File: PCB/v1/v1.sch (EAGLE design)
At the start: 64 parts, among them U2 AT24C512C-SHD-B

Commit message: push to work from main pc
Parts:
- removed R1, R2, R3, R4: (no value), resistor-shunt:BVS
- added R5, R6, R7, R8: (no value), eagle-ltspice:RR1206
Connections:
- net N$20: now also R7.1; no longer R1.2
- net N$36: now also R6.1; no longer R2.2
- net N$37: now also R7.2; no longer R1.1
- net N$38: now also R6.2; no longer R2.1
- net N$40: now also R8.1; no longer R4.2
- net N$45: now also R5.1; no longer R3.1
- net VDD: now also R5.2, R8.2; no longer R3.2, R4.1

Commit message: takes its time
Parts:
- removed PIO10, PIO11: (no value), wirepad:1,6/0,8
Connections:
- removed net N$42: PIO10.P, U$1.PIO[10]
- removed net N$47: PIO11.P, U$1.PIO[11]
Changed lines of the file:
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@@
 <part name="AIO0" library="wirepad" deviceset="1,6/0,8" device=""/>
 <part name="PIO3" library="wirepad" deviceset="1,6/0,8" device=""/>
-<part name="PIO10" library="wirepad" deviceset="1,6/0,8" device=""/>
-<part name="PIO11" library="wirepad" deviceset="1,6/0,8" device=""/>
 <part name="C1" library="AVX_By_element14_Batch_1" deviceset="UQCL2A100JAT2A/500" device="" value="1u"/>
 <part name="VPLUS" library="solpad" deviceset="LSP10" device="" value="Vrail"/>
@@
 <instance part="AIO0" gate="P" x="-55.88" y="15.24" rot="R90"/>
 <instance part="PIO3" gate="P" x="-33.02" y="10.16" rot="R90"/>
-<instance part="PIO10" gate="P" x="-20.32" y="81.28" rot="MR0"/>
-<instance part="PIO11" gate="P" x="-27.94" y="91.44" rot="R180"/>
 <instance part="C1" gate="A" x="73.152" y="108.204" rot="R90"/>
 <instance part="VPLUS" gate="1" x="-157.48" y="114.3" rot="R270"/>
@@
 </segment>
 </net>
-<net name="N$47" class="0">
-<segment>
-<pinref part="PIO11" gate="P" pin="P"/>
-<wire x1="-33.02" y1="91.44" x2="-30.48" y2="91.44" width="0.1524" layer="91"/>
-<pinref part="U$1" gate="G$1" pin="PIO[11]"/>
-</segment>
-</net>
 <net name="N$48" class="0">
 <segment>
@@
 </segment>
 </net>
-<net name="N$42" class="0">
-<segment>
-<pinref part="PIO10" gate="P" pin="P"/>
-<pinref part="U$1" gate="G$1" pin="PIO[10]"/>
-</segment>
-</net>

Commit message: getting there
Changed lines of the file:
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@@
 <wire x1="-129.54" y1="101.6" x2="-137.16" y2="101.6" width="0.1524" layer="91"/>
 <junction x="-137.16" y="101.6"/>
-<wire x1="-137.16" y1="101.6" x2="-144.78" y2="101.6" width="0.1524" layer="91"/>
 <pinref part="C19" gate="A" pin="C1"/>
 <wire x1="-154.94" y1="101.6" x2="-144.78" y2="101.6" width="0.1524" layer="91"/>
@@
 <junction x="-157.48" y="71.12"/>
 <pinref part="U$6" gate="G$1" pin="NEG"/>
+<wire x1="-144.78" y1="101.6" x2="-137.16" y2="101.6" width="0.1524" layer="91"/>
 </segment>
 <segment>

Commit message: quickly added antenna
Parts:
- added U$7: ANTENNA_1LEFT, ant-planar-1:ANTENNA_1LEFT
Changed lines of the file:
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@@
 <part name="R7" library="eagle-ltspice" deviceset="R" device="R1206"/>
 <part name="R8" library="eagle-ltspice" deviceset="R" device="R1206"/>
+<part name="U$7" library="ant-planar-1" deviceset="ANTENNA_1" device="LEFT"/>
 </parts>
 <sheets>
-<sheet>
-<plain>
-</plain>
-<instances>
-</instances>
-<busses>
-</busses>
-<nets>
-</nets>
-</sheet>
 <sheet>
 <plain>
@@
 <instance part="GND7" gate="1" x="-129.54" y="15.24"/>
 <instance part="C14" gate="A" x="-101.6" y="10.16" rot="R90"/>
-<instance part="GND9" gate="1" x="-165.1" y="27.94"/>
+<instance part="GND9" gate="1" x="-152.4" y="25.4"/>
 <instance part="C16" gate="A" x="-137.16" y="109.22" rot="R270"/>
 <instance part="C17" gate="A" x="-129.54" y="109.22" rot="R270"/>
@@
 <instance part="R7" gate="G$1" x="-48.26" y="-12.7" rot="R90"/>
 <instance part="R8" gate="G$1" x="30.48" y="-27.94" rot="R90"/>
+<instance part="U$7" gate="G$1" x="-157.48" y="45.72"/>
 </instances>
 <busses>
@@
 </segment>
 <segment>
+<pinref part="C10" gate="A" pin="C1"/>
+<pinref part="C11" gate="A" pin="C1"/>
+<wire x1="-137.16" y1="20.32" x2="-129.54" y2="20.32" width="0.1524" layer="91"/>
+<pinref part="GND7" gate="1" pin="GND"/>
+<wire x1="-129.54" y1="17.78" x2="-129.54" y2="20.32" width="0.1524" layer="91"/>
+<junction x="-129.54" y="20.32"/>
+<wire x1="-129.54" y1="20.32" x2="-121.92" y2="20.32" width="0.1524" layer="91"/>
+</segment>
+<segment>
 <pinref part="GND9" gate="1" pin="GND"/>
-<wire x1="-165.1" y1="35.56" x2="-165.1" y2="30.48" width="0.1524" layer="91"/>
+<wire x1="-152.4" y1="33.02" x2="-152.4" y2="27.94" width="0.1524" layer="91"/>
 </segment>
 <segment>
@@
 <wire x1="-83.82" y1="119.38" x2="-76.2" y2="119.38" width="0.1524" layer="91"/>
 <junction x="-76.2" y="119.38"/>
-</segment>
-<segment>
-<pinref part="C11" gate="A" pin="C1"/>
-<pinref part="C10" gate="A" pin="C1"/>
-<wire x1="-137.16" y1="20.32" x2="-129.54" y2="20.32" width="0.1524" layer="91"/>
-<pinref part="GND7" gate="1" pin="GND"/>
-<wire x1="-129.54" y1="20.32" x2="-121.92" y2="20.32" width="0.1524" layer="91"/>
-<wire x1="-129.54" y1="17.78" x2="-129.54" y2="20.32" width="0.1524" layer="91"/>
-<junction x="-129.54" y="20.32"/>
 </segment>
 </net>
@@
 <wire x1="-96.52" y1="35.56" x2="-109.22" y2="35.56" width="0.1524" layer="91"/>
 <pinref part="U$1" gate="G$1" pin="RF"/>
-</segment>
-</net>
+<wire x1="-109.22" y1="35.56" x2="-152.4" y2="35.56" width="0.1524" layer="91"/>
+<junction x="-109.22" y="35.56"/>
+</segment>
+</net>

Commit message: latest
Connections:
- net GND: now also U$5.NEG; no longer U$6.NEG
- net N$34: now also U$6.POS; no longer U$5.POS
- net N$48: now also U$5.POS, U$6.NEG; no longer U$5.NEG, U$6.POS
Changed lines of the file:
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@@
 <part name="U$2" library="MINI_SMT_8_PIN_CONNECTOR" deviceset="8PIN_SMT_CONNECTOR" device=""/>
 <part name="U$4" library="SSP-T7-F" deviceset="SSP-T7-F" device=""/>
-<part name="U$5" library="BATTERY_2996" deviceset="BATTERY_2996" device=""/>
-<part name="U$6" library="BATTERY_2996" deviceset="BATTERY_2996" device=""/>
 <part name="R5" library="eagle-ltspice" deviceset="R" device="R1206"/>
 <part name="R6" library="eagle-ltspice" deviceset="R" device="R1206"/>
@@
 <part name="R8" library="eagle-ltspice" deviceset="R" device="R1206"/>
 <part name="U$7" library="ant-planar-1" deviceset="ANTENNA_1" device="LEFT"/>
+<part name="U$5" library="BATTERY_2996" deviceset="BATTERY_2996" device=""/>
+<part name="U$6" library="BATTERY_2996" deviceset="BATTERY_2996" device=""/>
 </parts>
 <sheets>
@@
 <instance part="U$2" gate="G$1" x="43.18" y="-48.26"/>
 <instance part="U$4" gate="G$1" x="-109.22" y="69.85" rot="R270"/>
-<instance part="U$5" gate="G$1" x="-172.72" y="101.6"/>
-<instance part="U$6" gate="G$1" x="-172.72" y="78.74"/>
 <instance part="R5" gate="G$1" x="1.27" y="85.09"/>
 <instance part="R6" gate="G$1" x="-40.64" y="-12.7" rot="R90"/>
@@
 <instance part="R8" gate="G$1" x="30.48" y="-27.94" rot="R90"/>
 <instance part="U$7" gate="G$1" x="-157.48" y="45.72"/>
+<instance part="U$5" gate="G$1" x="-172.72" y="78.74"/>
+<instance part="U$6" gate="G$1" x="-172.72" y="101.6"/>
 </instances>
 <busses>
@@
 <pinref part="VGND" gate="1" pin="MP"/>
 <junction x="-157.48" y="71.12"/>
-<pinref part="U$6" gate="G$1" pin="NEG"/>
 <wire x1="-144.78" y1="101.6" x2="-137.16" y2="101.6" width="0.1524" layer="91"/>
+<pinref part="U$5" gate="G$1" pin="NEG"/>
 </segment>
 <segment>
@@
 <pinref part="U$1" gate="G$1" pin="VDD_PADS"/>
 <pinref part="U$1" gate="G$1" pin="VDD_BAT_SMPS"/>
-<pinref part="U$5" gate="G$1" pin="POS"/>
+<pinref part="U$6" gate="G$1" pin="POS"/>
 </segment>
 </net>
@@
 <segment>
 <wire x1="-162.56" y1="93.98" x2="-162.56" y2="86.36" width="0.1524" layer="91"/>
-<pinref part="U$5" gate="G$1" pin="NEG"/>
-<pinref part="U$6" gate="G$1" pin="POS"/>
-</segment>
-</net>
+<pinref part="U$5" gate="G$1" pin="POS"/>
+<pinref part="U$6" gate="G$1" pin="NEG"/>
+</segment>
+</net>

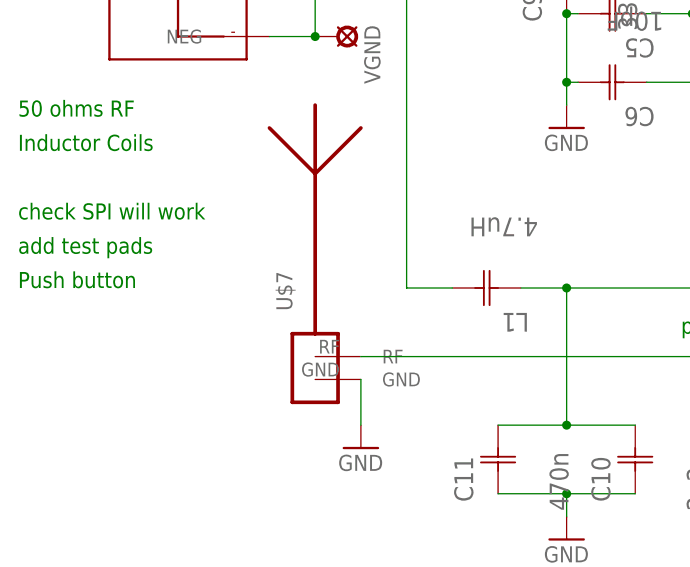
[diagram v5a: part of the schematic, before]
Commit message: expose pads more and add other ADC
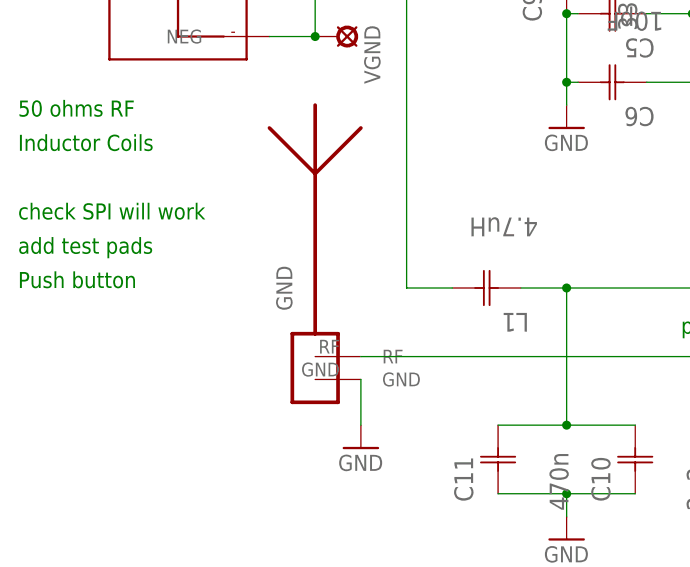
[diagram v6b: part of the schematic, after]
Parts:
- renumbered U$7 to GND
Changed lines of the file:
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@@
 <part name="R7" library="eagle-ltspice" deviceset="R" device="R1206"/>
 <part name="R8" library="eagle-ltspice" deviceset="R" device="R1206"/>
-<part name="U$7" library="ant-planar-1" deviceset="ANTENNA_1" device="LEFT"/>
+<part name="GND" library="ant-planar-1" deviceset="ANTENNA_1" device="LEFT"/>
 <part name="U$5" library="BATTERY_2996" deviceset="BATTERY_2996" device=""/>
 <part name="U$6" library="BATTERY_2996" deviceset="BATTERY_2996" device=""/>
@@
 <instance part="R7" gate="G$1" x="-48.26" y="-12.7" rot="R90"/>
 <instance part="R8" gate="G$1" x="30.48" y="-27.94" rot="R90"/>
-<instance part="U$7" gate="G$1" x="-157.48" y="45.72"/>
+<instance part="GND" gate="G$1" x="-157.48" y="45.72"/>
 <instance part="U$5" gate="G$1" x="-172.72" y="78.74"/>
 <instance part="U$6" gate="G$1" x="-172.72" y="101.6"/>

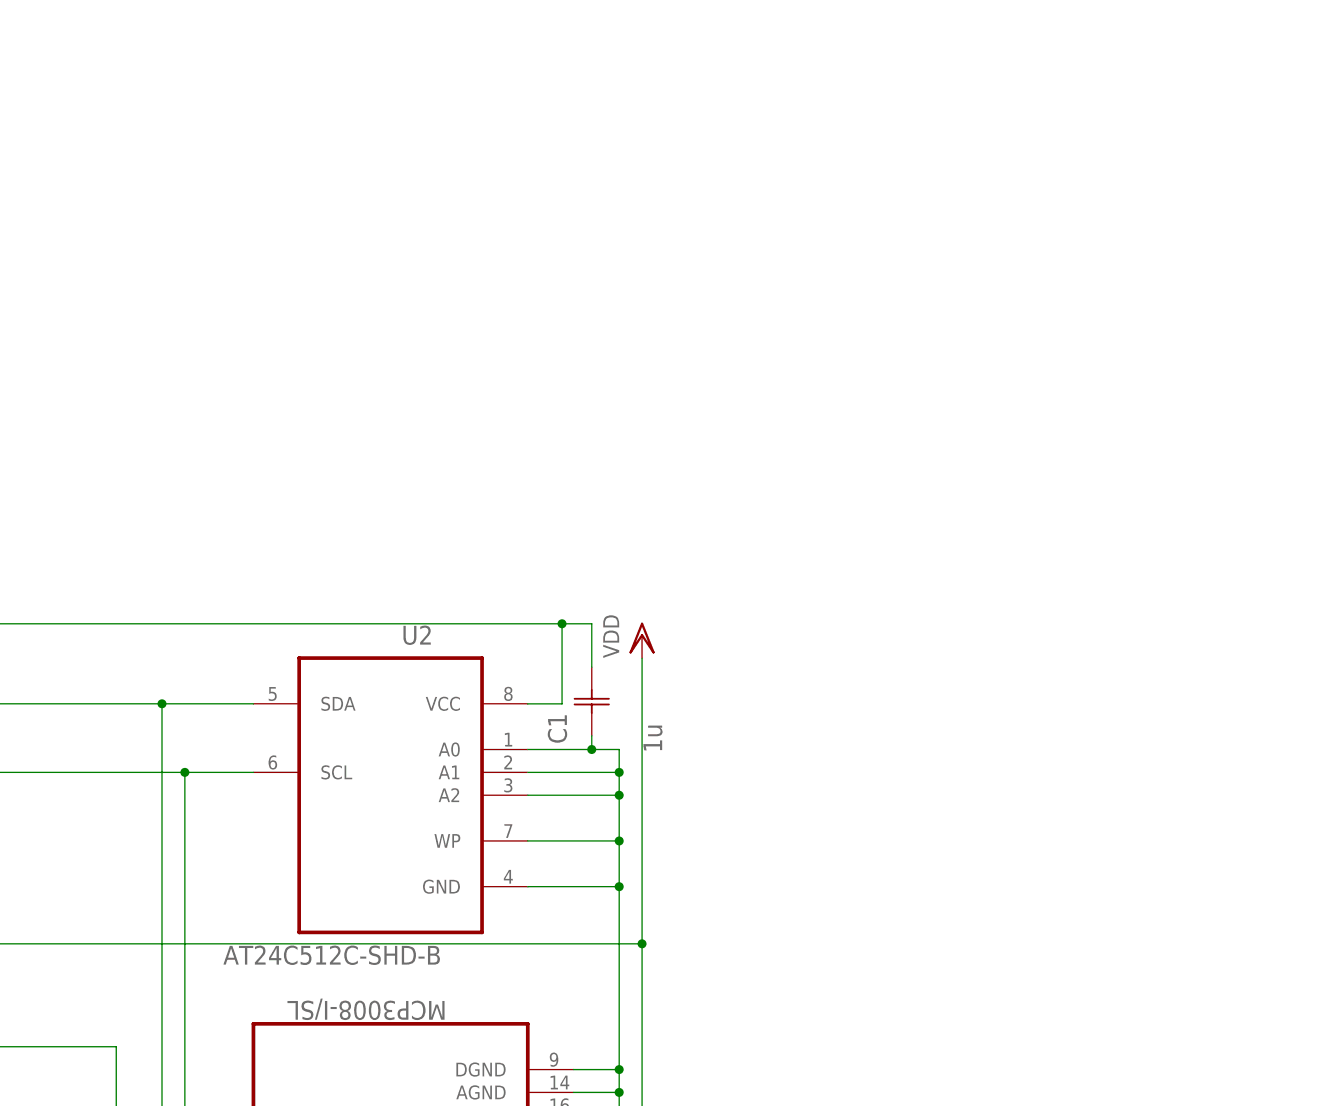
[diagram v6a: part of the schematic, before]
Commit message: added new chip, brought out solder mask. Need to check crystal pads and ground connections
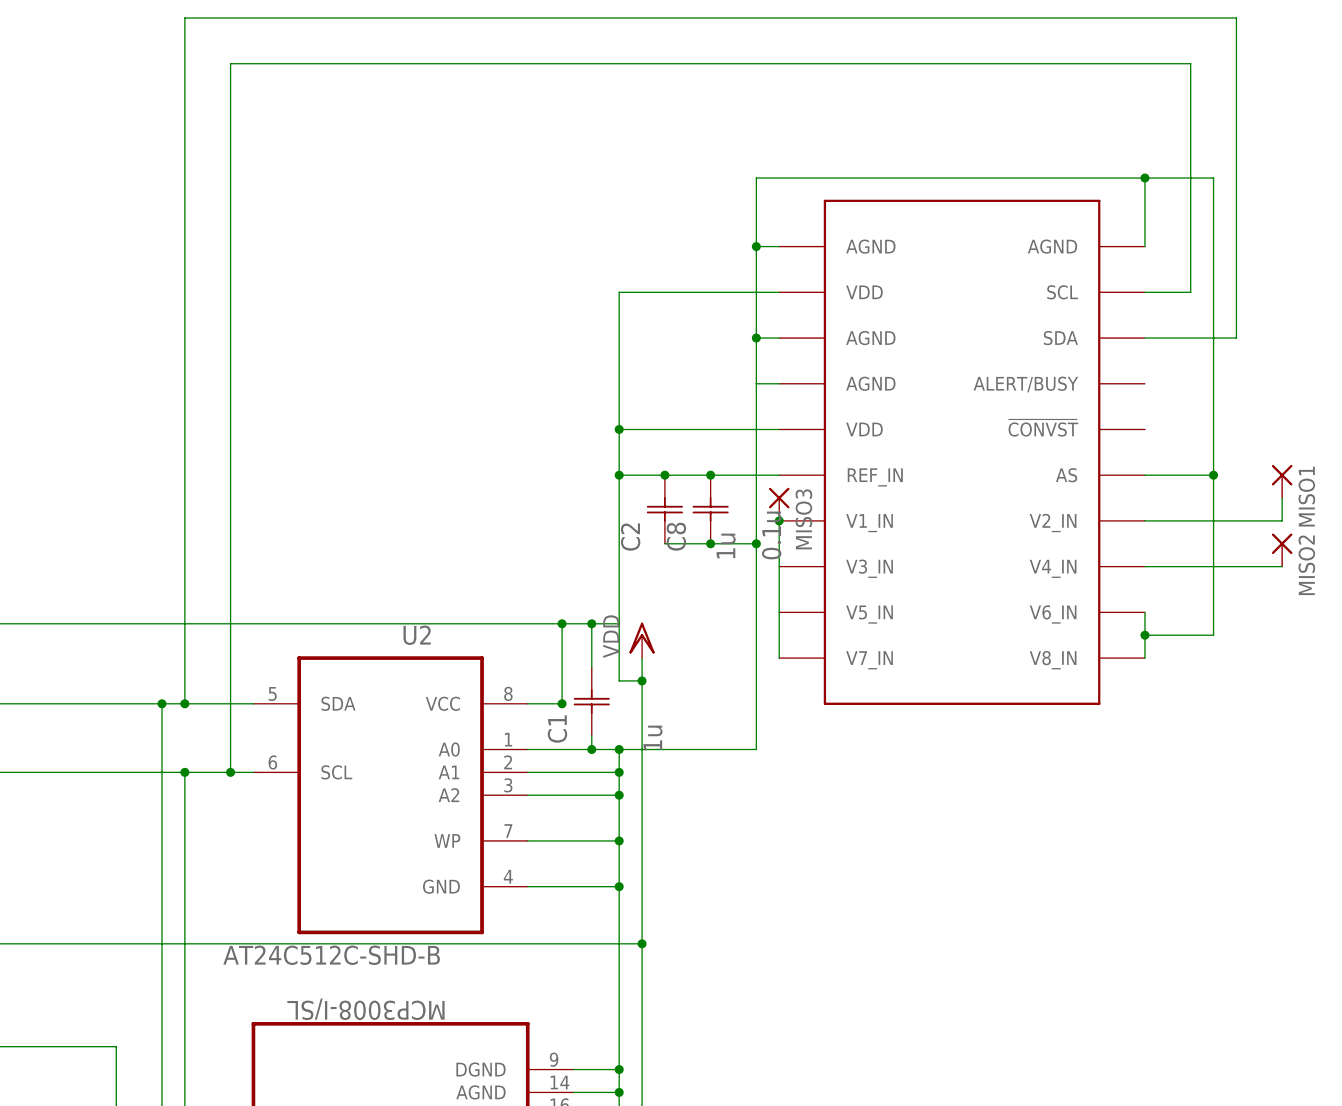
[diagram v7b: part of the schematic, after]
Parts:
- added C2: 1u, AVX_By_element14_Batch_1:UQCL2A100JAT2A/500
- added C8: 0.1u, AVX_By_element14_Batch_1:UQCL2A100JAT2A/500
- added MISO1, MISO2, MISO3: (no value), wirepad:1,6/0,8
- added U$7: AD7997, AD7997:AD7997
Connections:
- net N$28 renamed VDD_CORE
- removed net N$21: ADC0.CLK, ADC1.CLK, SCL.P, U$1.I2C_SCL, U2.SCL
- removed net N$22: ADC0.DOUT, ADC1.DOUT, SDA.P, U$1.I2C_SDA, U2.SDA
- removed net N$46: C1.C2, MEMPWR.P, U$1.PIO[2]
- new net N$86: MISO1.P, U$7.V2_IN
- new net N$87: MISO2.P, U$7.V4_IN
- new net N$88: MISO3.P, U$7.V1_IN, U$7.V7_IN
- new net N$90: U$7.V6_IN, U$7.V8_IN
- new net SCL: ADC0.CLK, ADC1.CLK, SCL.P, U$1.I2C_SCL, U$7.SCL, U2.SCL
- new net SDA: ADC0.DOUT, ADC1.DOUT, SDA.P, U$1.I2C_SDA, U$7.SDA, U2.SDA
- net GND: now also C2.C1, C8.C1, U$7.AGND@1, U$7.AGND@2, U$7.AGND@3, U$7.AGND@4, U$7.AS
- net VDD: now also C1.C2, C2.C2, C8.C2, MEMPWR.P, U$1.PIO[2], U$7.REF_IN, U$7.VDD@1, U$7.VDD@2, U2.VCC
